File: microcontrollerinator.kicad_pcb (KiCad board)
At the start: 2 copper layers, 46 parts, among them J1 USB_C_Receptacle_USB2.0_14P, J2 Conn_01x20, J3 Conn_01x20, J4 Conn_01x03, J5 Conn_01x03, Q1 AO3401A, SW1 SW_Push, U1 RP2040, U2 MCP1700x-330xxTT, U3 W25Q128JVS, U4 BQ21040DBV, Y1 12MHz

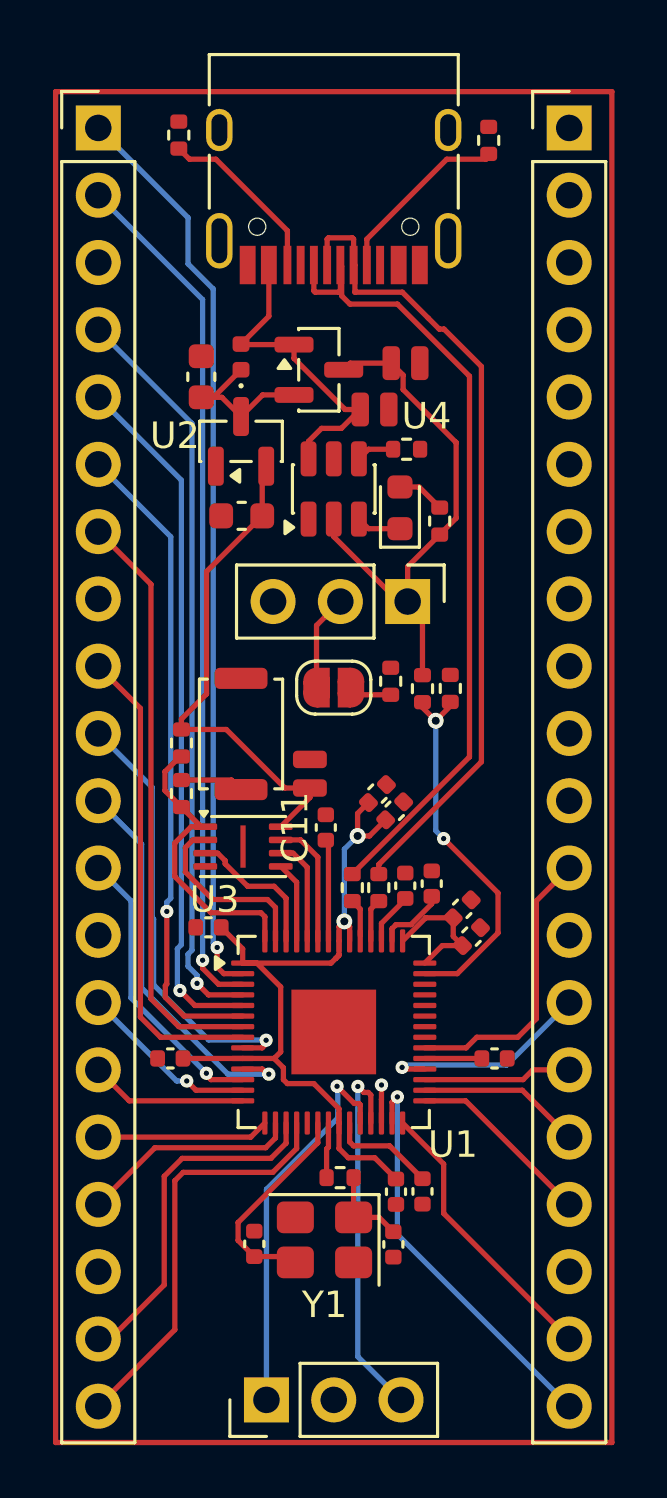
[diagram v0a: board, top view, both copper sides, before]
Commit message: finished routing pcb
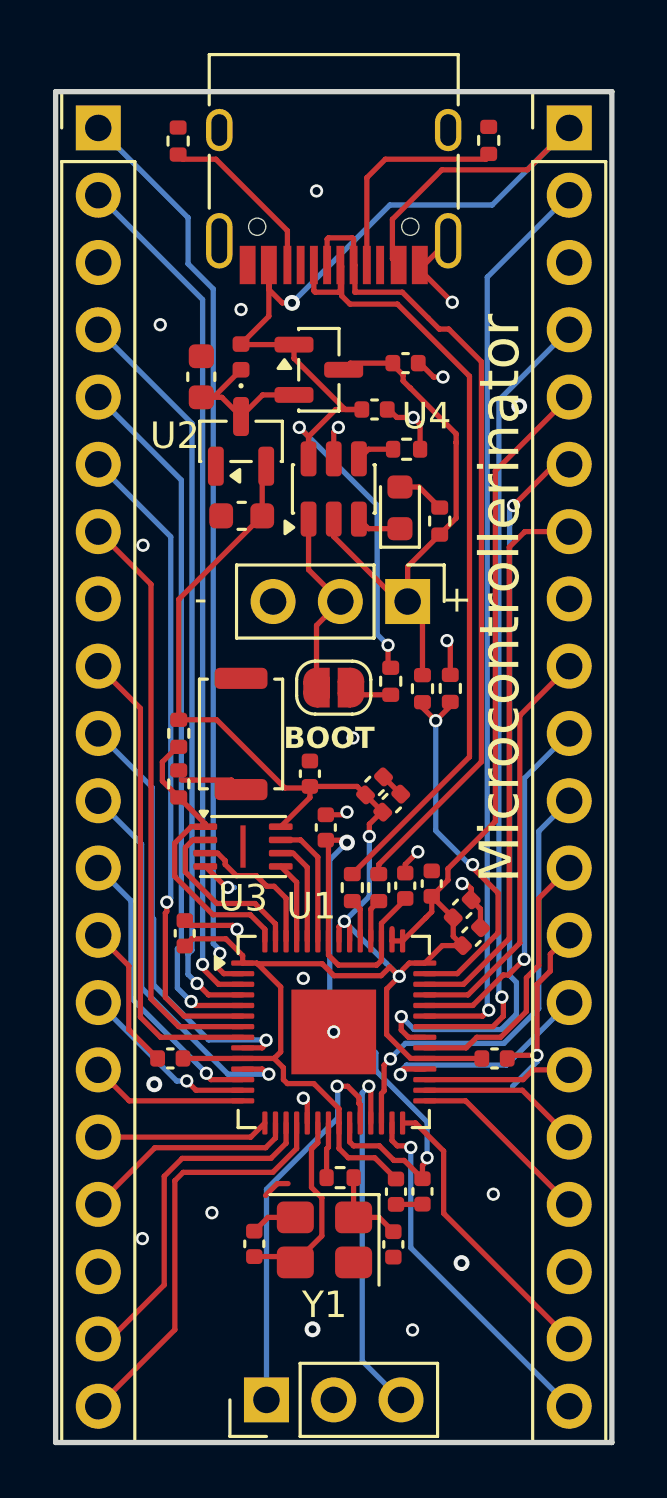
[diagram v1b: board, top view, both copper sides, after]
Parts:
- added G***: LOGO, LOGO, B.Cu at (141.7, 99.5)
- C17, C18, C19: footprint Capacitor_SMD:C_0504_1310Metric -> Capacitor_SMD:C_0402_1005Metric
- moved C1 0.92 mm to (135.9, 106.8), turned to 90 degrees
- moved R7 0.38 mm to (135.7, 99.2)
- moved R6 0.38 mm to (135.7, 101.1)
- moved C2 0.31 mm to (143.7, 101.9)
- moved C3 0.31 mm to (143.0, 101.2)
- moved R2 0.23 mm to (135.6, 76.9)
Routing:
- net VBUS: track 12.4 -> 49.4 mm, vias 0 -> 3
- net GND: track 0.00 -> 34.9 mm, vias 0 -> 27
- net /GPIO25: track 0.00 -> 34.8 mm, vias 0 -> 1
- net +3V3: track 58.8 -> 91.3 mm, vias 2 -> 3
- net /GPIO24: track 0.00 -> 30.5 mm, vias 0 -> 1
- net /GPIO23: track 0.00 -> 29.0 mm, vias 0 -> 2
- net /GPIO28_ADC2: track 0.00 -> 21.2 mm
- net +1V1: track 9.86 -> 28.8 mm, vias 0 -> 2
- net /RUN: track 1.44 -> 17.3 mm
- net /GPIO27_ADC1: track 0.00 -> 15.6 mm
- net /GPIO26_ADC0: track 0.00 -> 13.7 mm, vias 0 -> 1
- net /BAT_TS: track 3.62 -> 7.23 mm
- net /GPIO16: track 15.4 -> 13.7 mm
- net Net-(J1-CC1): track 7.01 -> 8.37 mm
- net (no net): track 0.00 -> 1.04 mm
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- added copper zone on B.Cu, net GND
- added copper zone on F.Cu, net GND
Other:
- board outline added: 21 x 51 mm
- board text added: "+"
- board text added: "-"
- board text added: "BOOT"
- board text added: "Microcontrollerinator"

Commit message: added production files
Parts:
- R11: value 2K -> 1K
- R12: value 7K -> 3.2K
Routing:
- net (no net): track 1.04 -> 0.00 mm
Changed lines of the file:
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@@
 			(outputformat 1)
 			(mirror no)
-			(drillshape 1)
+			(drillshape 0)
 			(scaleselection 1)
-			(outputdirectory "")
+			(outputdirectory "production/")
 		)
 	)
@@
 			)
 		)
-		(property "Value" "2K"
+		(property "Value" "1K"
 			(at 0 1.17 90)
 			(layer "F.Fab")
@@
 			)
 			(rotate
-				(xyz 0 0 0)
+				(xyz -0 -180 -0)
 			)
 		)
@@
 		(tags "SOT TO_SOT_SMD")
 		(property "Reference" "U2"
-			(at 0.2125 -2.5 180)
+			(at 0.1775 -2.625 180)
 			(layer "F.SilkS")
 			(effects
@@
 			)
 			(rotate
-				(xyz 0 0 0)
+				(xyz -0 -180 -0)
 			)
 		)
@@
 			)
 		)
-		(property "Value" "7K"
+		(property "Value" "3.2K"
 			(at 0 1.17 90)
 			(layer "F.Fab")
@@
 	)
 	(segment
-		(start 139.375 116.225)
-		(end 138.925 116.675)
-		(width 0.2)
-		(layer "F.Cu")
-		(net 0)
-	)
-	(segment
-		(start 139.775 116.225)
-		(end 139.375 116.225)
-		(width 0.2)
-		(layer "F.Cu")
-		(net 0)
-	)
-	(segment
 		(start 135.9 111.41)
 		(end 135.81 111.5)
@@
 	)
 	(segment
-		(start 146.121 88.237404)
-		(end 146.121 88.25)
-		(width 0.2)
-		(layer "F.Cu")
-		(net 8)
-	)
-	(segment
-		(start 146.121 88.25)
-		(end 146.121 91.1015)
-		(width 0.2)
-		(layer "F.Cu")
-		(net 8)
-	)
-	(segment
 		(start 144.85 97.03)
 		(end 144.85 94.81)
@@
 	)
 	(segment
-		(start 143.67 85.25)
-		(end 142.125 85.25)
+		(start 146.121 91.1015)
+		(end 146.121 87.921)
 		(width 0.2)
 		(layer "F.Cu")
@@
 	)
 	(segment
-		(start 146.121 88.25)
-		(end 146.121 87.921)
+		(start 143.67 85.25)
+		(end 142.125 85.25)
 		(width 0.2)
 		(layer "F.Cu")

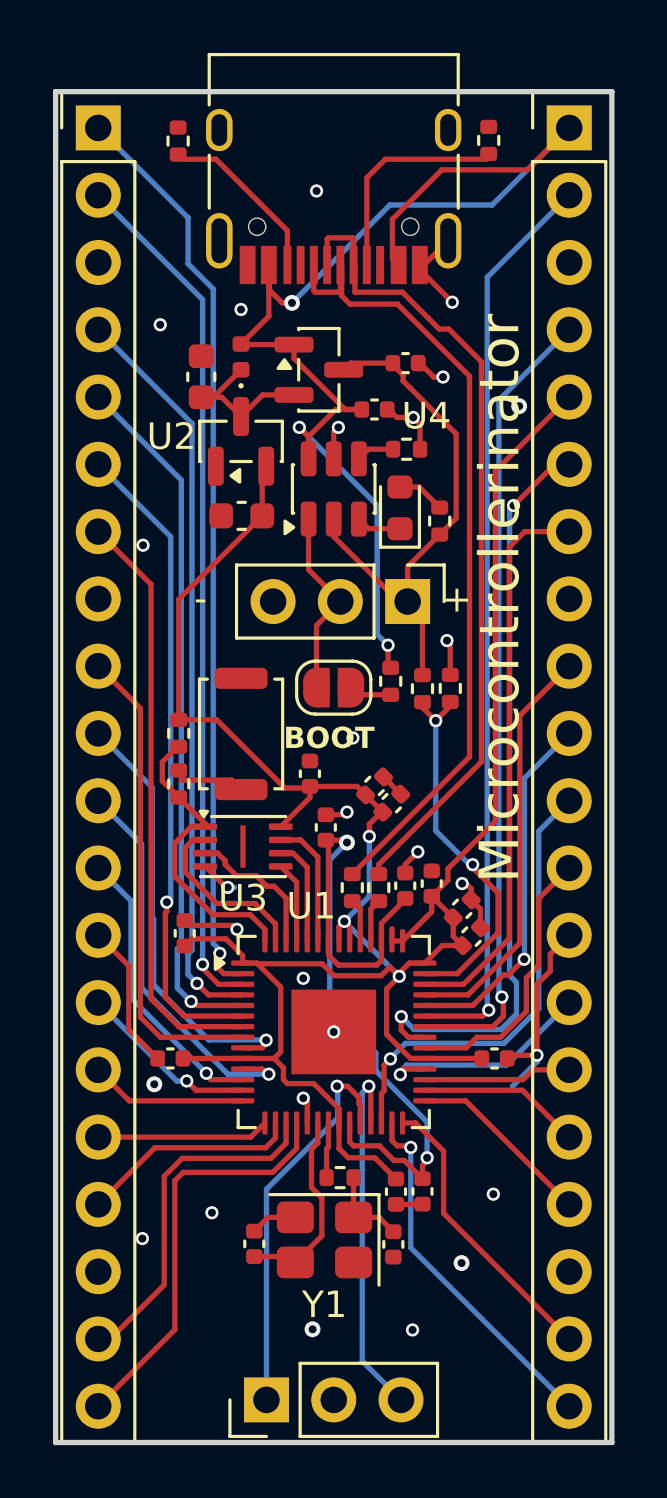
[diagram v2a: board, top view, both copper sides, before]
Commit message: fixed 3d model
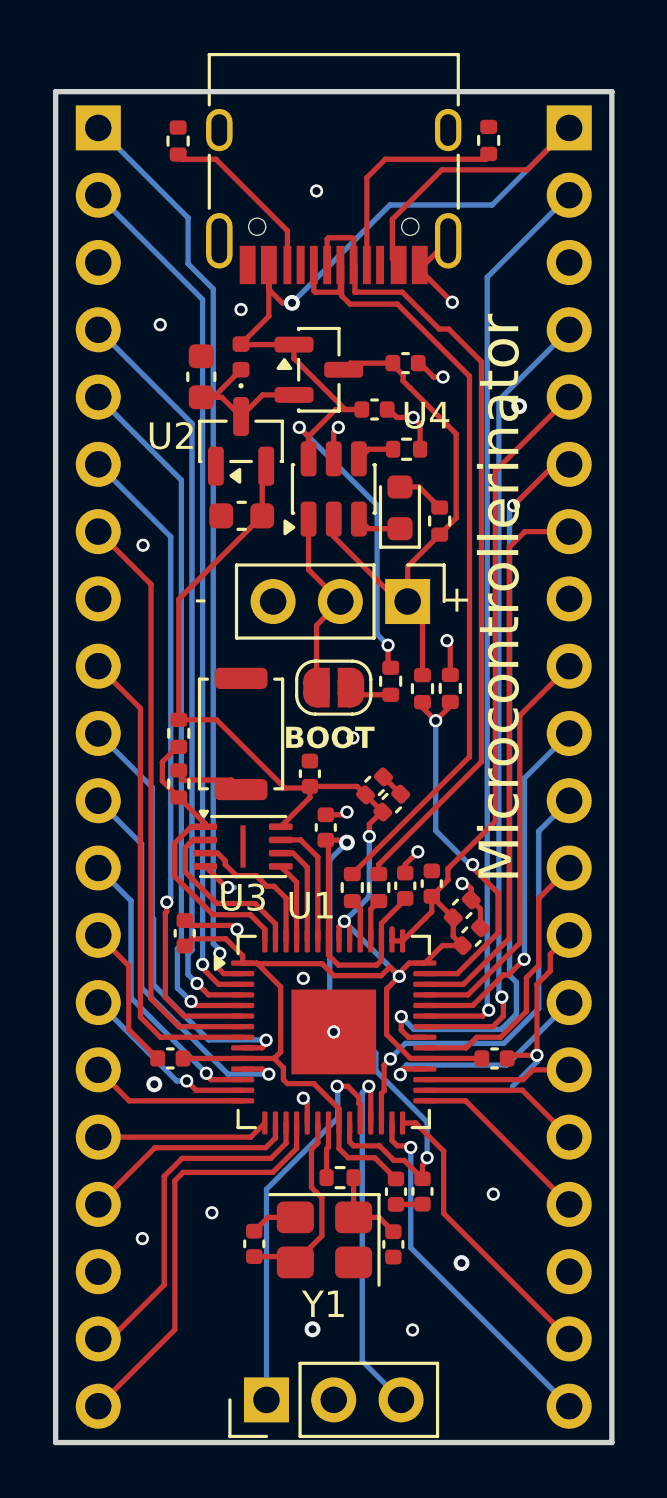
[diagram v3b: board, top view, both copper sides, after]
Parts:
- J2, J3: moved to B.Cu
- turned J2 to 180 degrees
- turned J3 to 180 degrees
